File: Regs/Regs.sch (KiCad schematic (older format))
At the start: 110 parts, among them J1 Conn_01x08_Female, J10 Conn_01x08_Male, J11 Conn_01x02_Male, J12 Conn_01x02_Male, J13 Conn_01x08_Male, J14 Conn_01x01_Male, J15 Screw_Terminal_01x02, J2 Conn_01x08_Female, J3 Conn_01x08_Female, J4 Conn_01x08_Female, J5 Conn_01x08_Female, J6 Conn_01x08_Female, J7 Conn_01x08_Female, J8 Conn_01x08_Female, J9 Conn_01x03_Male, U1 74LS573, U10 74HC238, U11 74LS257, U12 74LS00, U13 74LS257, U14 74LS257, U15 74LS00, U2 74LS573, U3 74LS573, U4 74LS573, U5 74LS573, U6 74LS573, U7 74LS573, U8 74LS573, U9 74LS00

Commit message: Regs pcb is ready
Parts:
- removed U12: 74LS00, Package_DIP:DIP-14_W7.62mm_Socket, symbol 74xx:74LS00
- removed unit 2 of U15
- added unit 4 of U15
- added unit 3 of U15
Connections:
- net 8\16: now also U15.1, U15.2
- net DST0: now also U15.12; no longer U15.1
- net GND: now also U10.4 (~G2A); no longer U10.5 (~G2B)
- net ~Bank0: now also U10.5 (~G2B); no longer U10.4 (~G2A)
- net at U10.1 (A0): now also U15.8
- net at U13.1 (S): now also U15.3, U15.13; no longer U15.2
- new net: U15.10, U15.11, U15.9
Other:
- moved on the sheet: U15A
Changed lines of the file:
@@
 L7
 Wire Wire Line
-	6250 7025 6475 7025
-Text Label 6250 7025 0    50   ~ 0
+	6250 7175 6475 7175
+Text Label 6250 7175 0    50   ~ 0
 ~Bank0
 $Comp
 L power:GND #PWR029
 U 1 1 63156ED1
-P 6475 7175
-F 0 "#PWR029" H 6475 6925 50  0001 C CNN
-F 1 "GND" V 6480 7047 50  0000 R CNN
-F 2 "" H 6475 7175 50  0001 C CNN
-F 3 "" H 6475 7175 50  0001 C CNN
-	1    6475 7175
+P 6475 7025
+F 0 "#PWR029" H 6475 6775 50  0001 C CNN
+F 1 "GND" V 6480 6897 50  0000 R CNN
+F 2 "" H 6475 7025 50  0001 C CNN
+F 3 "" H 6475 7025 50  0001 C CNN
+	1    6475 7025
 	0    1    1    0
 $EndComp
@@
 Wire Wire Line
 	4175 7475 4175 7575
-$Comp
-L 74xx:74LS00 U12
-U 3 1 63913429
-P 4475 7575
-F 0 "U12" H 4475 7258 50  0000 C CNN
-F 1 "74LS00" H 4475 7349 50  0000 C CNN
-F 2 "Package_DIP:DIP-14_W7.62mm_Socket" H 4475 7575 50  0001 C CNN
-F 3 "http://www.ti.com/lit/gpn/sn74ls00" H 4475 7575 50  0001 C CNN
-	3    4475 7575
-	1    0    0    1
-$EndComp
 Text Label 3925 7575 0    50   ~ 0
 8\16
@@
 $Comp
 L 74xx:74LS00 U15
-U 2 1 63EA4D2E
-P 5925 7575
-F 0 "U15" H 5925 7900 50  0000 C CNN
-F 1 "74LS00" H 5925 7809 50  0000 C CNN
-F 2 "Package_DIP:DIP-14_W7.62mm_Socket" H 5925 7575 50  0001 C CNN
-F 3 "http://www.ti.com/lit/gpn/sn74ls00" H 5925 7575 50  0001 C CNN
-	2    5925 7575
-	1    0    0    -1
-$EndComp
-$Comp
-L 74xx:74LS00 U15
 U 1 1 63EA6F3B
-P 5325 7475
-F 0 "U15" H 5325 7800 50  0000 C CNN
-F 1 "74LS00" H 5325 7709 50  0000 C CNN
-F 2 "Package_DIP:DIP-14_W7.62mm_Socket" H 5325 7475 50  0001 C CNN
-F 3 "http://www.ti.com/lit/gpn/sn74ls00" H 5325 7475 50  0001 C CNN
-	1    5325 7475
+P 4475 7575
+F 0 "U15" H 4475 7900 50  0000 C CNN
+F 1 "74LS00" H 4475 7809 50  0000 C CNN
+F 2 "Package_DIP:DIP-14_W7.62mm_Socket" H 4475 7575 50  0001 C CNN
+F 3 "http://www.ti.com/lit/gpn/sn74ls00" H 4475 7575 50  0001 C CNN
+	1    4475 7575
 	1    0    0    -1
 $EndComp
@@
 	1    0    0    -1
 $EndComp
+$Comp
+L 74xx:74LS00 U15
+U 4 1 62778A83
+P 5325 7475
+F 0 "U15" H 5325 7800 50  0000 C CNN
+F 1 "74LS00" H 5325 7709 50  0000 C CNN
+F 2 "Package_DIP:DIP-14_W7.62mm_Socket" H 5325 7475 50  0001 C CNN
+F 3 "http://www.ti.com/lit/gpn/sn74ls00" H 5325 7475 50  0001 C CNN
+	4    5325 7475
+	1    0    0    -1
+$EndComp
+$Comp
+L 74xx:74LS00 U15
+U 3 1 627D3F6D
+P 5925 7575
+F 0 "U15" H 5925 7900 50  0000 C CNN
+F 1 "74LS00" H 5925 7809 50  0000 C CNN
+F 2 "Package_DIP:DIP-14_W7.62mm_Socket" H 5925 7575 50  0001 C CNN
+F 3 "http://www.ti.com/lit/gpn/sn74ls00" H 5925 7575 50  0001 C CNN
+	3    5925 7575
+	1    0    0    -1
+$EndComp

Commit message: Polishing Regs
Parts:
- removed unit 2 of U9
- added C9: 1uF, Capacitor_THT:C_Disc_D5.0mm_W2.5mm_P5.00mm, symbol Device:C
- added D65, D66: LED, LED_THT:LED_Rectangular_W5.0mm_H2.0mm, symbol Device:LED
- added H1, H2, H3, H4: MountingHole, MountingHole:MountingHole_3.2mm_M3, symbol Mechanical:MountingHole
- added R1, R2, R3, R4: 1k, Resistor_THT:R_Axial_DIN0207_L6.3mm_D2.5mm_P10.16mm_Horizontal, symbol Device:R
- added U12: 74LS10, Package_DIP:DIP-14_W7.62mm_Socket, symbol 74xx:74LS10
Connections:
- net 8\16: now also R4.1
- net Bank0-cmd: now also U9.9; no longer U9.13
- net Bank1-cmd: now also U9.13; no longer U9.9
- net GND: now also C9.2, R4.2, U12.7 (GND)
- net VCC: now also R1.2, R2.1, R3.1, U12.14 (VCC)
- net ~Bank0: now also D66.1 (K), U12.12
- net ~Bank1: now also D65.1 (K), U12.1
- net at U9.8: now also U12.2
- new net: C9.1, R1.1, U12.13
- new net: D65.2 (A), R2.2
- new net: D66.2 (A), R3.2
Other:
- moved on the sheet: C1, C2, C3, C4, C5, C6, C7, C8

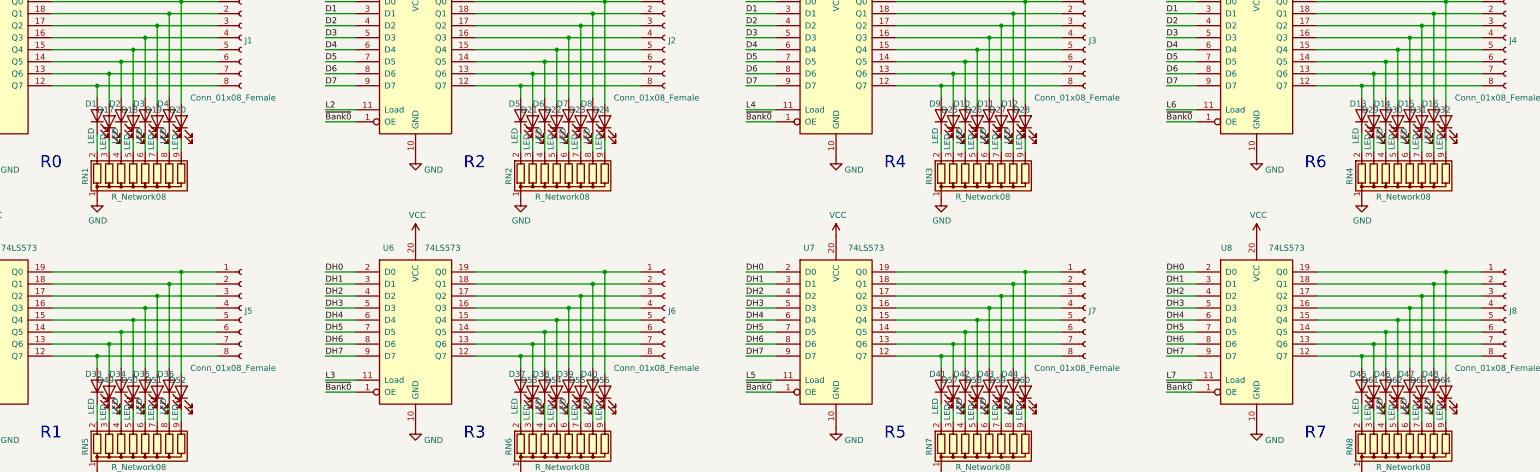
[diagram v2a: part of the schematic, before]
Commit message: Mark LEDs like HLx
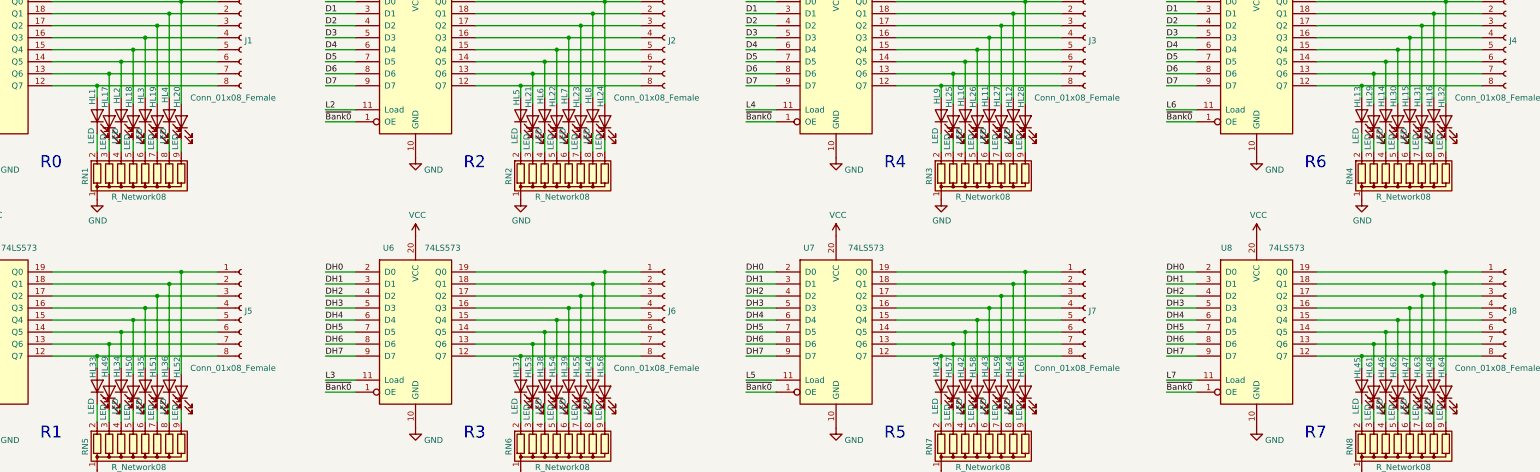
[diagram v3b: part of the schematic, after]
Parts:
- renumbered D1 to HL1, D10 to HL10, D11 to HL11, D12 to HL12, D13 to HL13, D14 to HL14, D15 to HL15, D16 to HL16, D17 to HL17, D18 to HL18, D19 to HL19, D2 to HL2, D20 to HL20, D21 to HL21, D22 to HL22, D23 to HL23, D24 to HL24, D25 to HL25, D26 to HL26, D27 to HL27, D28 to HL28, D29 to HL29, D3 to HL3, D30 to HL30, D31 to HL31, D32 to HL32, D33 to HL33, D34 to HL34, D35 to HL35, D36 to HL36, D37 to HL37, D38 to HL38, D39 to HL39, D4 to HL4, D40 to HL40, D41 to HL41, D42 to HL42, D43 to HL43, D44 to HL44, D45 to HL45, D46 to HL46, D47 to HL47, D48 to HL48, D49 to HL49, D5 to HL5, D50 to HL50, D51 to HL51, D52 to HL52, D53 to HL53, D54 to HL54, D55 to HL55, D56 to HL56, D57 to HL57, D58 to HL58, D59 to HL59, D6 to HL6, D60 to HL60, D61 to HL61, D62 to HL62, D63 to HL63, D64 to HL64, D7 to HL7, D8 to HL8, D9 to HL9

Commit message: Prepare to add Bank1
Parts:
- added J16, J18, J19: Conn_01x08_Male, Connector_PinHeader_2.54mm:PinHeader_1x08_P2.54mm_Vertical, symbol Connector:Conn_01x08_Male
- added J17: Conn_01x01_Male, Connector_PinHeader_2.54mm:PinHeader_1x01_P2.54mm_Vertical, symbol Connector:Conn_01x01_Male
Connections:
- net D0: now also J18.1 (Pin_1)
- net D1: now also J18.2 (Pin_2)
- net D2: now also J18.3 (Pin_3)
- net D3: now also J18.4 (Pin_4)
- net D4: now also J18.5 (Pin_5)
- net D5: now also J18.6 (Pin_6)
- net D6: now also J18.7 (Pin_7)
- net D7: now also J18.8 (Pin_8)
- net DH0: now also J16.1 (Pin_1), J19.1 (Pin_1)
- net DH1: now also J16.2 (Pin_2), J19.2 (Pin_2)
- net DH2: now also J16.3 (Pin_3), J19.3 (Pin_3)
- net DH3: now also J16.4 (Pin_4), J19.4 (Pin_4)
- net DH4: now also J16.5 (Pin_5), J19.5 (Pin_5)
- net DH5: now also J16.6 (Pin_6), J19.6 (Pin_6)
- net DH6: now also J16.7 (Pin_7), J19.7 (Pin_7)
- net DH7: now also J16.8 (Pin_8), J19.8 (Pin_8)
- net ~Bank1: now also J17.1 (Pin_1)
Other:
- moved on the sheet: H1, H2, H3, H4, J10, J13, J15, U15E

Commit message: Regs polisnig
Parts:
- removed unit 1 of U12
- removed unit 1 of U9
- added R5: 1k, Resistor_THT:R_Axial_DIN0207_L6.3mm_D2.5mm_P10.16mm_Horizontal, symbol Device:R
- added SW1, SW2: SW_Push, Button_Switch_THT:SW_PUSH_6mm_H4.3mm, symbol Switch:SW_Push
- added unit 3 of U12
- added unit 2 of U12
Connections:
- net Bank0-cmd: now also U9.10; no longer U9.9
- net Bank1-cmd: now also U9.12; no longer U9.13
- net C2: now also U9.13, U9.9; no longer U9.10, U9.12
- net GND: now also SW1.1, SW2.1
- net VCC: now also R5.1
- net ~Bank0: now also U12.6, U12.9
- net ~Bank1: now also U12.3, U12.8
- net at C9.1, R1.1: now also SW2.2, U12.4
- net at U9.8: now also U12.5
- net at U9.11: now also U12.11
- new net: R5.2, SW1.2, U12.10
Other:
- moved on the sheet: C9, J17, R1, U12D, U9C, U9D, U9E
